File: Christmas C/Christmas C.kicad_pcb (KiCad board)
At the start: 2 copper layers, 94.2 x 94.2 mm, 15 parts, among them J1 A_LEFT, J2 A_RIGHT, J3 B_LEFT, J4 B_RIGHT, J5 PWR_EXT, M1 Mounting, M2 Mounting, M3 Mounting, M4 Mounting, SW1 SELECT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

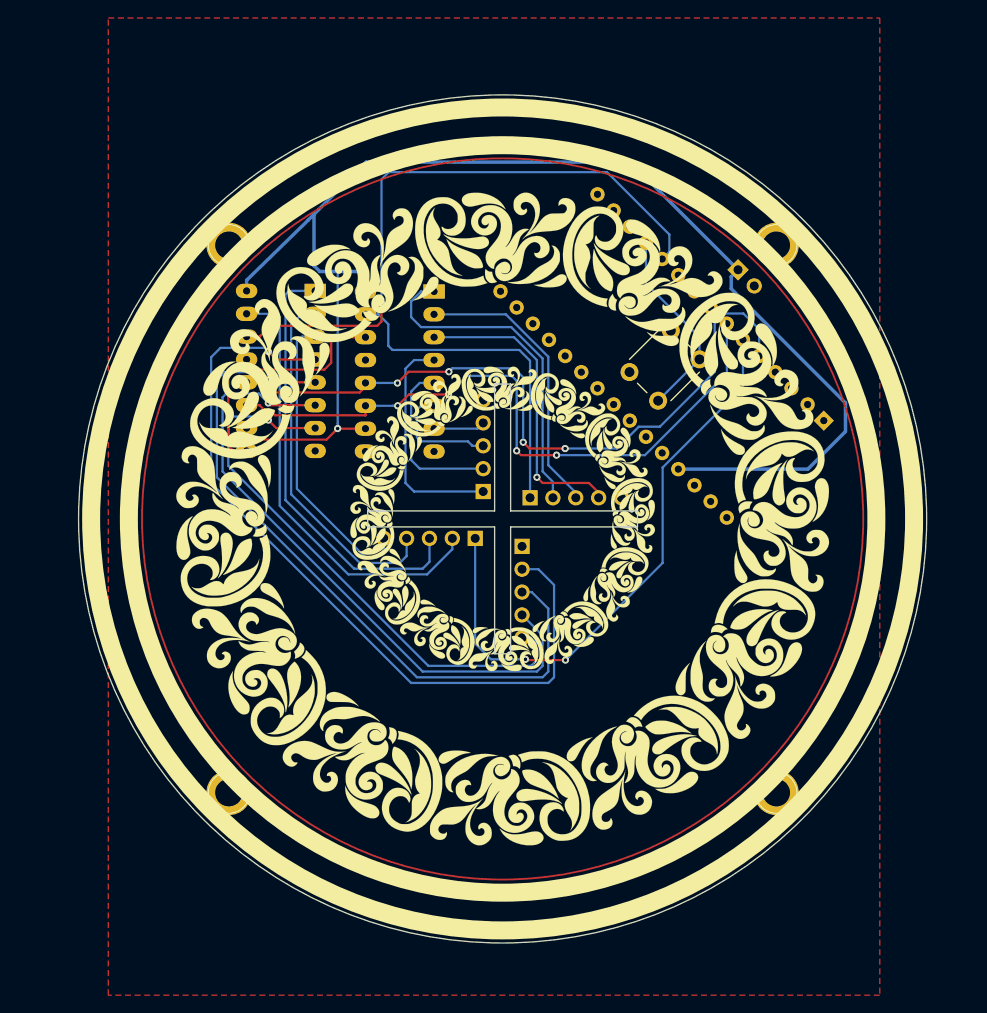
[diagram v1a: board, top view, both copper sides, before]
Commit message: Tweaked bottom connectors
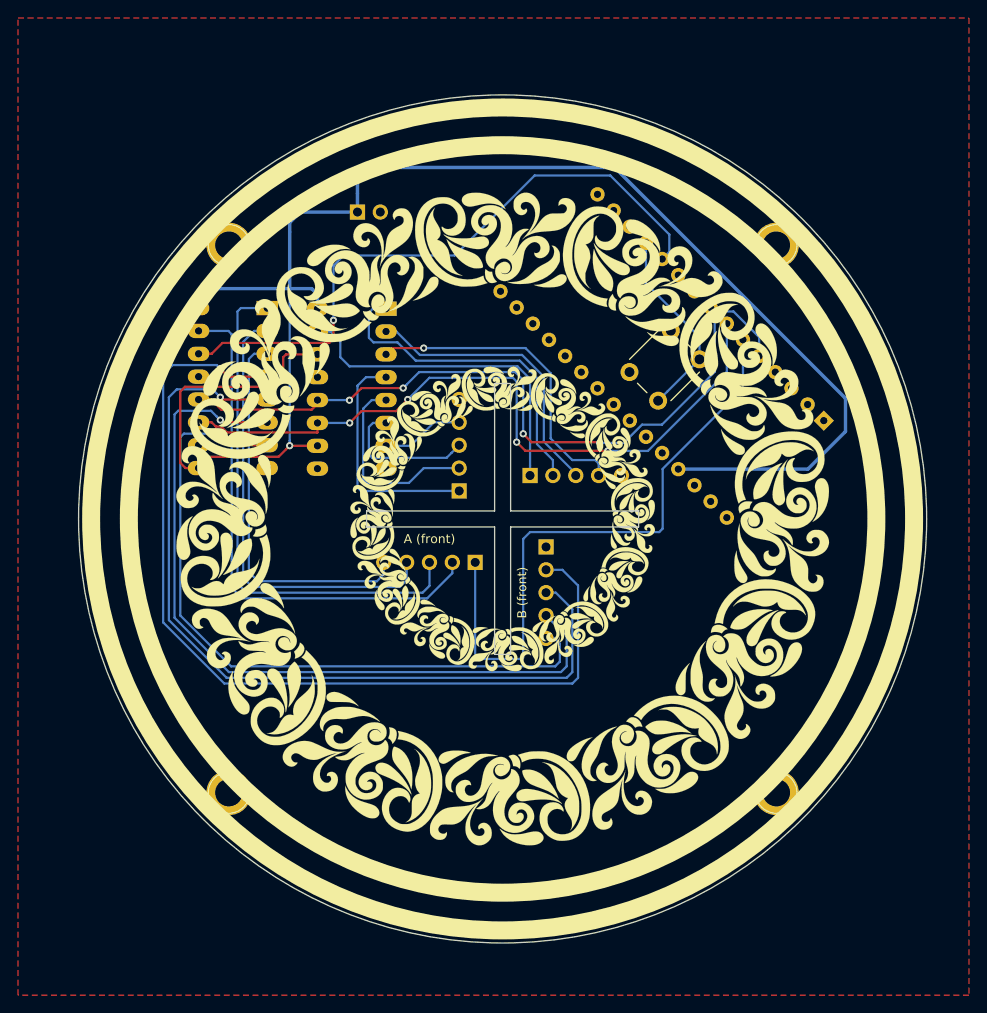
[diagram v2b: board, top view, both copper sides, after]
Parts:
- moved J5 42.8 mm to (88.6, 116.6), turned to 270 degrees
- moved U1 5.66 mm to (78.6, 127.3)
- moved U2 5.66 mm to (91.8, 127.3)
- moved J3 2.67 mm to (109.6, 153.8)
- moved J4 2.67 mm to (99.9, 147.6)
- moved J1 2.67 mm to (101.7, 155.5)
- moved J2 2.48 mm to (107.8, 145.9)
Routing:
- net Net-(J3-Pad5): track 62.8 -> 78.7 mm
- net Net-(J3-Pad4): track 70.9 -> 86.5 mm
- net Net-(J3-Pad3): track 79.5 -> 94.9 mm
- net Net-(J3-Pad2): track 88.6 -> 103.8 mm
- net Net-(J1-Pad5): track 33.0 -> 43.0 mm
- net Net-(J1-Pad4): track 40.3 -> 50.3 mm
- net Net-(J1-Pad3): track 48.4 -> 58.4 mm
- net Net-(J1-Pad2): track 49.5 -> 59.4 mm
- net /SH_CLOCK: track 73.7 -> 78.6 mm
- net /SH_LATCH: track 79.9 -> 84.2 mm
- net /STAR: track 66.2 -> 69.7 mm, vias 2 -> 0
- net Net-(J4-Pad4): track 5.72 -> 9.21 mm
- net Net-(J4-Pad2): track 19.0 -> 22.3 mm
- net Net-(J4-Pad3): track 12.9 -> 15.9 mm
- net +5V: track 155.9 -> 157.5 mm
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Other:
- outline, holes or cut-outs redrawn
- board text added: "A (front)"
- board text added: "B (front)"

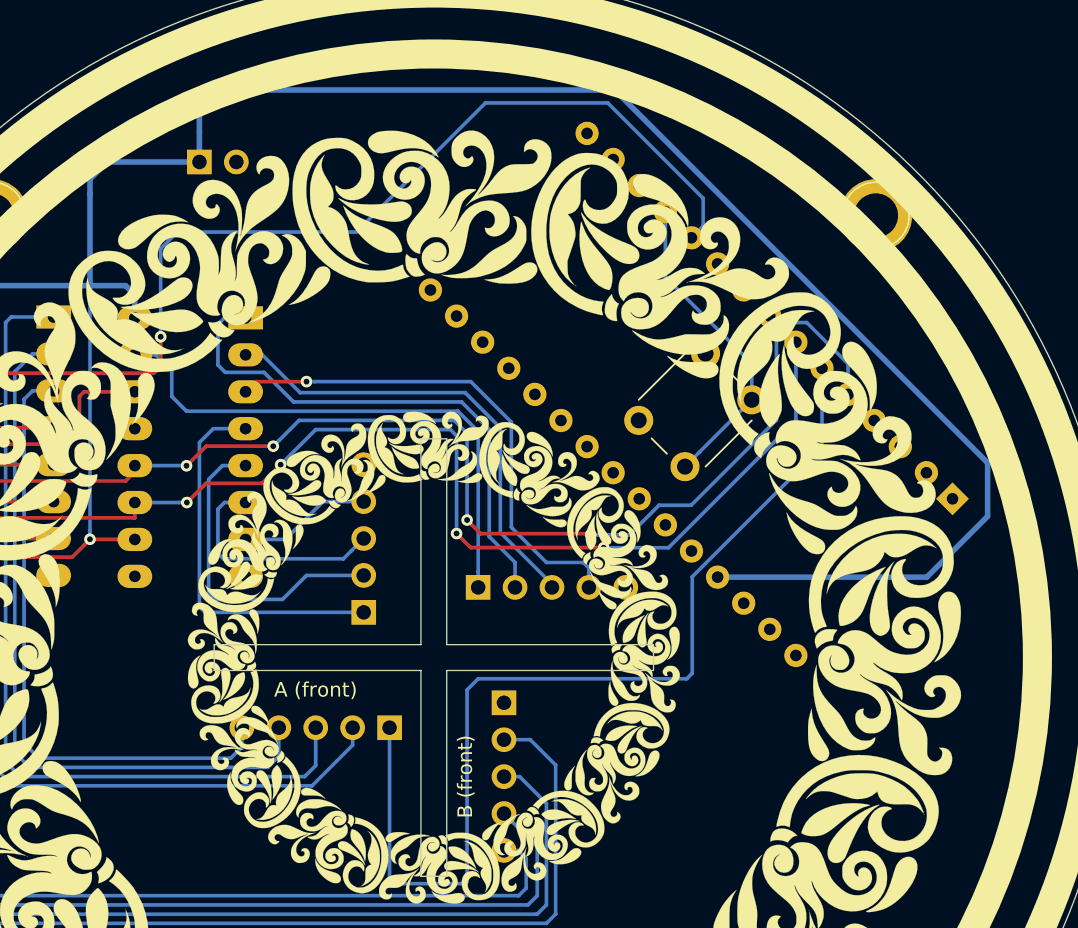
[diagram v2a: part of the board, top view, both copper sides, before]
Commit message: Changed Nano footprint to something standard
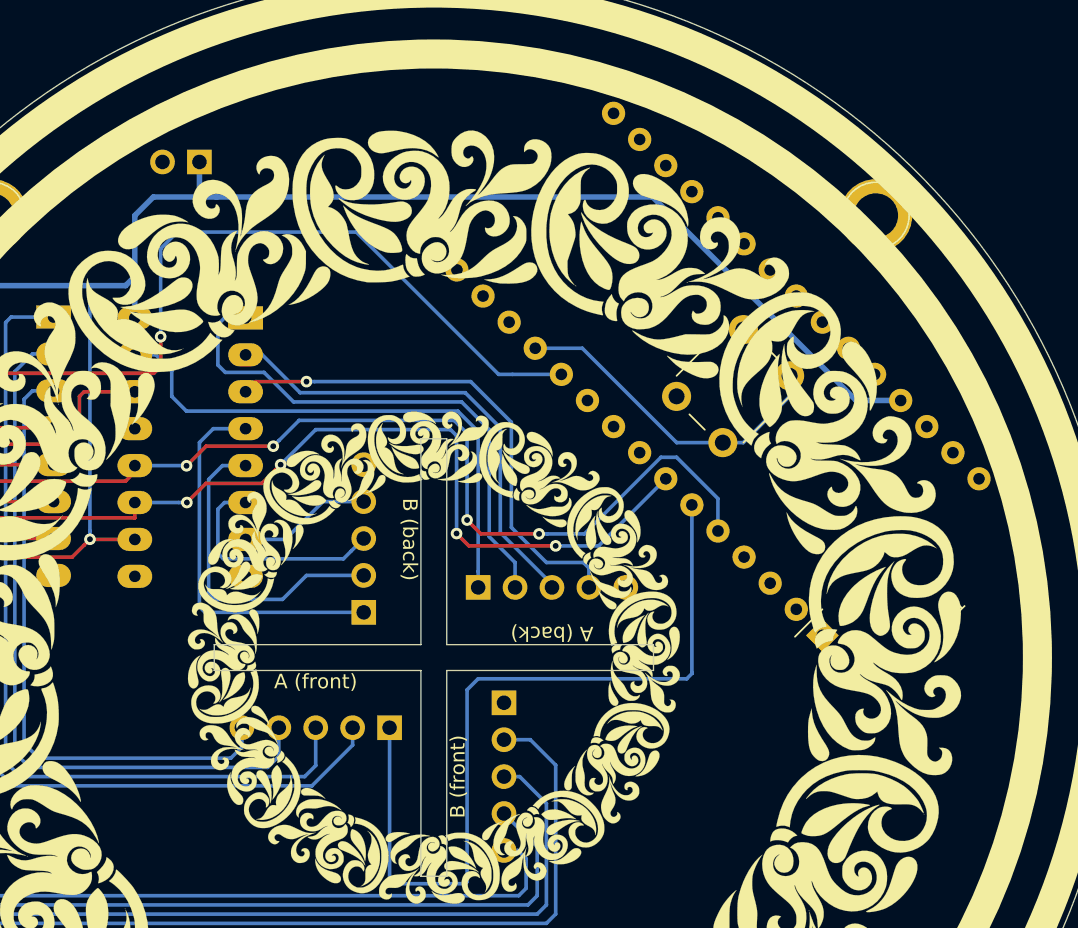
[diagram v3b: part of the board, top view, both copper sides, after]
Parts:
- A1: moved to B.Cu
- moved A1 13.0 mm to (131.5, 149.2), turned to 45 degrees
- moved SW1 3.08 mm to (121.5, 132.7)
- turned J5 to 90 degrees
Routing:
- net +5V: track 157.5 -> 116.2 mm
- net /SH_CLOCK: track 78.6 -> 62.5 mm
- net /SH_LATCH: track 84.2 -> 68.1 mm
- net /SH_DATA: track 71.0 -> 55.9 mm
- net /STAR: track 69.7 -> 56.7 mm
- net /SW_SEL: track 21.9 -> 22.9 mm
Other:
- board text added: "A (back)"
- board text added: "B (back)"
